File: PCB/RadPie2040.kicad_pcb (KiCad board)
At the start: 2 copper layers, 30 x 53.4 mm, 42 parts, among them J1 USB_C_Receptacle_USB2.0, J2 SWD, J6 Conn_01x16, J7 Conn_01x16, SW1 SW_BOOTSEL, SW2 SW_RESET, U1 W25Q128JVSIQ, U2 RP2040, U4 XC6206PxxxMR-Regulator_Linear, X1 12MHz

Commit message: Add pull-up for Flash, just in case
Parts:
- added R12: 5k1, Resistor_SMD:R_0402_1005Metric, F.Cu at (190.2, 51.0)
- moved C1 0.64 mm to (189.1, 52.1), turned to 180 degrees
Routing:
- net +3V3: track 108.0 -> 109.1 mm

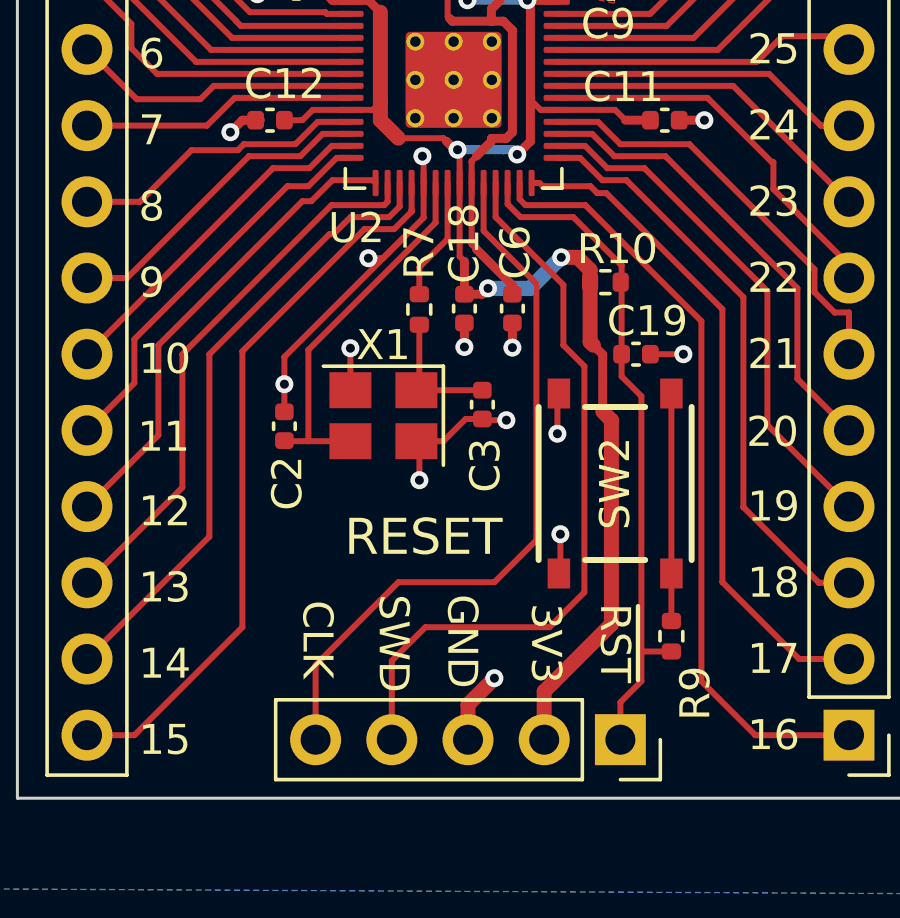
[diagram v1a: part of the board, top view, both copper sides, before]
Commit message: Refactor schematic to be hierarchical
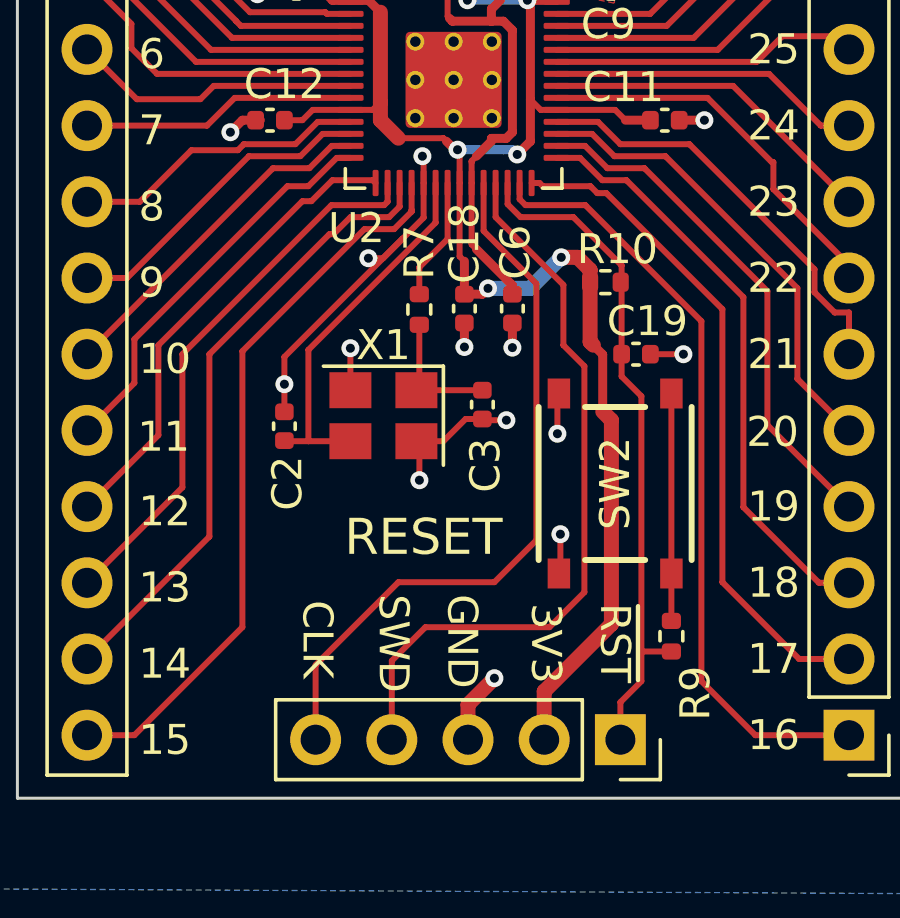
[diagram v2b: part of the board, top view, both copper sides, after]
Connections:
- net /CC1 renamed /USBC/CC1
- net /CC2 renamed /USBC/CC2
- net /USB_DT+ renamed /RP2040/USB_DT+
- net /USB_DT- renamed /RP2040/USB_DT-
- net CS renamed /CS
- net QSPI_CLK renamed /RP2040/QSPI_CLK
- net SD0 renamed /RP2040/SD0
- net SD1 renamed /RP2040/SD1
- net SD2 renamed /RP2040/SD2
- net SD3 renamed /RP2040/SD3
- net SWCLK renamed /SWCLK
- net SWD renamed /SWD
- net USB_D+ renamed /USB_D+
- net USB_D- renamed /USB_D-
- net ~{RESET} renamed /~{RESET}

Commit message: jlcpcb production fixes
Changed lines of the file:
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@@
 			(size 1.125 1.75)
 			(layers "F.Cu" "F.Paste" "F.Mask")
-			(roundrect_rratio 0.222222)
+			(roundrect_rratio 0.2222222222)
 			(net 6 "VBUS")
 			(pintype "passive")
@@
 			(size 1.125 1.75)
 			(layers "F.Cu" "F.Paste" "F.Mask")
-			(roundrect_rratio 0.222222)
+			(roundrect_rratio 0.2222222222)
 			(net 5 "+5V")
 			(pintype "passive")
@@
 			(size 1.084435 1.084435)
 			(layers "F.Paste")
-			(roundrect_rratio 0.230535)
+			(roundrect_rratio 0.2305347946)
 		)
 		(pad "" smd roundrect
@@
 			(size 1.084435 1.084435)
 			(layers "F.Paste")
-			(roundrect_rratio 0.230535)
+			(roundrect_rratio 0.2305347946)
 		)
 		(pad "" smd roundrect
@@
 			(size 1.084435 1.084435)
 			(layers "F.Paste")
-			(roundrect_rratio 0.230535)
+			(roundrect_rratio 0.2305347946)
 		)
 		(pad "" smd roundrect
@@
 			(size 1.084435 1.084435)
 			(layers "F.Paste")
-			(roundrect_rratio 0.230535)
+			(roundrect_rratio 0.2305347946)
 		)
 		(pad "1" smd roundrect
@@
 			)
 		)
+		(property "JLCPCB Rotation Offset" "90"
+			(at 0 0 0)
+			(unlocked yes)
+			(layer "F.Fab")
+			(hide yes)
+			(effects
+				(font
+					(size 1 1)
+					(thickness 0.15)
+				)
+			)
+		)
 		(property ki_fp_filters "TO-???* *_Diode_* *SingleDiode* D_*")
 		(sheetname "USBC")
@@
 			(layer "F.Fab")
 			(hide yes)
+			(effects
+				(font
+					(size 1 1)
+					(thickness 0.15)
+				)
+			)
+		)
+		(property "JLCPCB Position Offset" "0,1.42"
+			(at 0 0 180)
+			(unlocked yes)
+			(layer "F.Fab")
+			(hide yes)
